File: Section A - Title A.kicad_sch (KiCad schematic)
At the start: 31 parts, among them J1 Screw_Terminal_01x04, Q2 HY1707, Q3 S8050, Q4 HY1707, U1 UC2843AQD8R

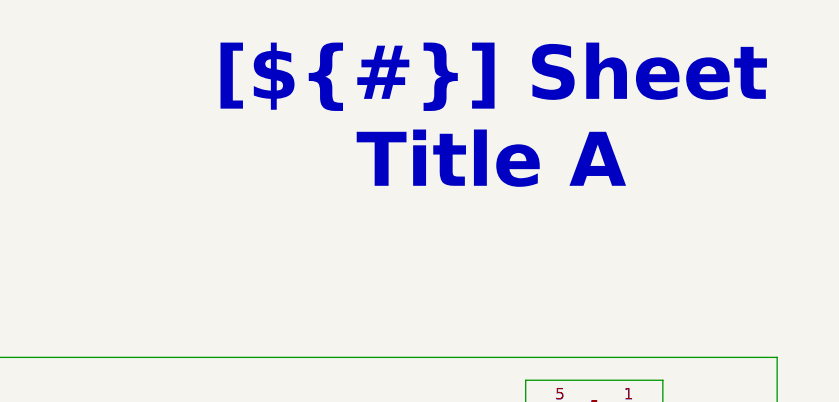
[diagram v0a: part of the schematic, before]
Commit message: New 3D path for trafo
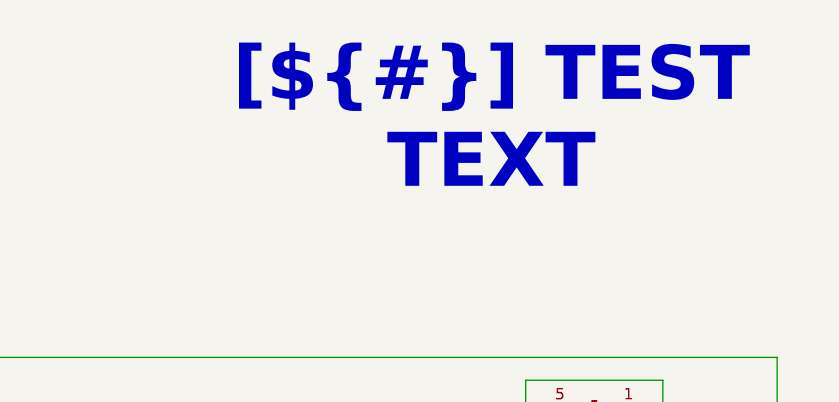
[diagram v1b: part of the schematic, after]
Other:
- title: Sheet Title A -> TEST TEXT
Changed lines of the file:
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@@
 	(paper "A4")
 	(title_block
-		(title "Sheet Title A")
+		(title "TEST TEXT")
 		(date "2025-01-12")
 		(rev "${REVISION}")
